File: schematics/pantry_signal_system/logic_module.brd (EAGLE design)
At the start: 45.7 x 53 mm, 24 parts, among them J5 JST-XH254-3P, J6 JST-XH254-2P, J7 JST-XH254-2P, Q4 STP14NM50N, Q5 2N3904, U10 FAN73611, U11 ATMEGA328P, U12 E220-900T22D, U13 BME280BME280-CONNECTOR-ONLY, U14 2004A I2C

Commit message: 1. Fixed issues in boards and firmwares
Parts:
- added J10: USBASP_PIN, my_devices:USBASP_PIN
- moved R24 13.0 mm to (63.5, 48.3), turned to 180 degrees
- moved FS1 8.03 mm to (67.3, 53.3), turned to 180 degrees
- moved FS2 4.02 mm to (58.4, 53.3)
- moved R23 2.54 mm to (45.7, 69.8)
- moved R26 1.27 mm to (63.5, 44.5)
- moved U13 1.27 mm to (68.6, 64.8)
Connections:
- removed net N$7: C9.P$1, R21.P$1, U11.PC6
- new net RESET: C9.P$1, J10.RST, R21.P$1, U11.PC6
- new net SERIAL_RX: J10.RXD, U11.PD1
- new net SERIAL_TX: J10.TXD, U11.PD0
- net +5V: now also J10.VCC
- net GND: now also J10.GND, J10.GND1
- net I2C2_SCL: now also J10.SCK
- net I2C2_SDA: now also J10.MISO
- net I2C_SCL: now also U11.PC5; no longer U11.PC4
- net I2C_SDA: now also U11.PC4; no longer U11.PC5
- net OPEN_DOOR_ALARM: now also J10.MOSI
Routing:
- net I2C2_SCL: track 9.20 -> 50.9 mm
- net RESET: track 0.00 -> 40.8 mm
- net I2C2_SDA: track 5.61 -> 43.9 mm
- net OPEN_DOOR_ALARM: track 22.5 -> 60.4 mm
- net SERIAL_TX: track 0.00 -> 34.2 mm, vias 0 -> 1
- net N$7: track 20.4 -> 0.00 mm
- net SERIAL_RX: track 0.00 -> 19.4 mm, vias 0 -> 1
- net GND: track 186.3 -> 175.3 mm
- net FLOODING_ALARM_OUTDOOR: track 12.5 -> 23.2 mm
- net I2C_SDA: track 15.5 -> 21.9 mm
- net +5V: track 135.9 -> 142.2 mm
- net LORA_RX: track 11.7 -> 16.5 mm
- net FLOODING_ALARM_INDOOR: track 14.1 -> 16.1 mm
- net I2C_SCL: track 19.6 -> 18.6 mm
- net ENABLE_DISPLAY: track 19.1 -> 19.9 mm
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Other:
- board text added: "REQ"
- board text added: "TX"

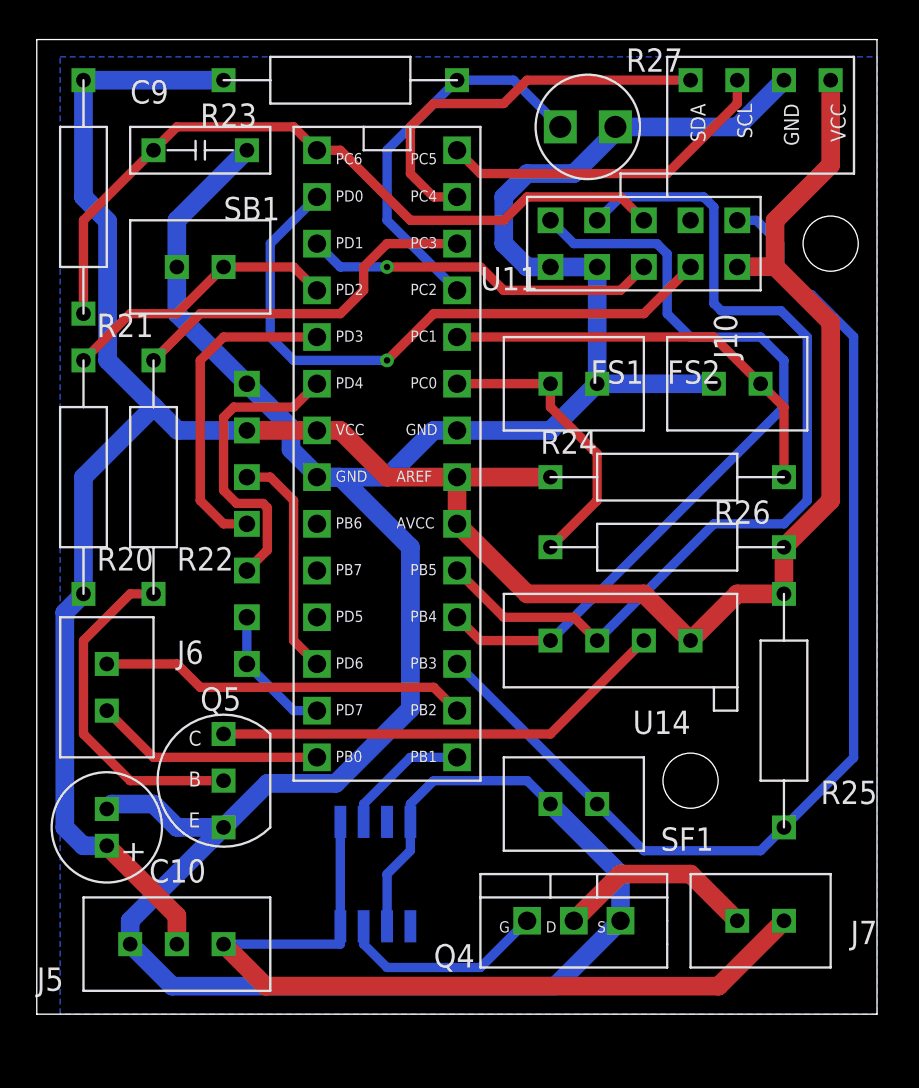
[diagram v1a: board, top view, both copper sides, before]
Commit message: Changes in schematics, changes in source code. Current version works too, but I changed boards to fix some possible errors
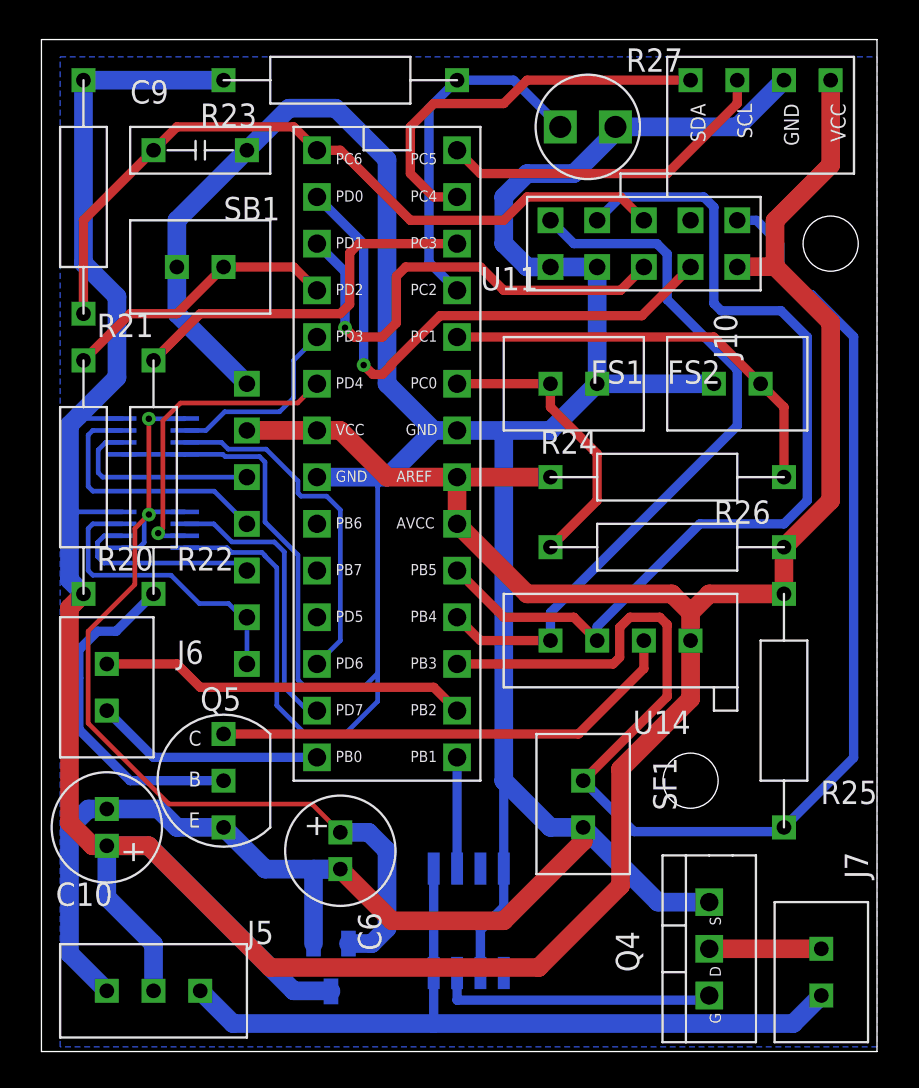
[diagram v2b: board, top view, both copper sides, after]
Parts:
- added C6: 10 uF, my_devices:C-MINI-5X7
- added U2, U3: SN74LVC2T45DCUR, my_devices:VSSOP-8
- added U7: MCP1703T-3302E/CB, my_devices:SOT-23A
- moved Q4 7.52 mm to (65.8, 22.6), turned to 90 degrees
- moved U10 5.68 mm to (52.1, 24.1)
- moved J7 4.33 mm to (71.9, 21.3), turned to 90 degrees
- moved J5 2.84 mm to (35.6, 20.3)
- moved SF1 0.51 mm to (58.9, 30.5), turned to 270 degrees
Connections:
- new net 3V3: C6.PLUS, U2.P1, U2.P5, U3.P1, U7.P2
- new net N$1: U12.TX, U3.P7
- new net N$2: U12.RX, U2.P6
- new net N$3: U12.AUX, U3.P6
- new net N$9: U12.M0, U12.M1, U2.P7
- net +5V: now also U2.P8, U3.P8, U7.P3
- net GND: now also C6.MINUS, U2.P4, U3.P4, U3.P5, U7.P1
- net LORA_AUX: now also U3.P3; no longer U12.AUX
- net LORA_M0M1: now also U2.P2; no longer U12.M0, U12.M1
- net LORA_RX: now also U2.P3; no longer U12.RX
- net LORA_TX: now also U3.P2; no longer U12.TX
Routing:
- net GND: track 175.3 -> 247.8 mm
- net +5V: track 142.2 -> 205.6 mm
- net 3V3: track 0.00 -> 50.6 mm, vias 0 -> 2
- net N$9: track 0.00 -> 16.6 mm
- net N$1: track 0.00 -> 14.2 mm
- net OPEN_DOOR_ALARM: track 60.4 -> 74.0 mm
- net N$3: track 0.00 -> 10.9 mm
- net N$2: track 0.00 -> 10.7 mm
- net LORA_M0M1: track 7.40 -> 15.7 mm
- net LORA_TX: track 17.6 -> 10.5 mm
- net LORA_AUX: track 12.5 -> 19.3 mm
- net SERIAL_RX: track 19.4 -> 25.8 mm
- net N$4: track 11.0 -> 6.10 mm
- net I2C2_SDA: track 43.9 -> 39.5 mm
- net N$6: track 11.4 -> 15.3 mm
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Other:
- board size 45.7 x 53 mm -> 45.4 x 55 mm

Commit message: Debugging logic module firmware, estabilishing LoRa connection....
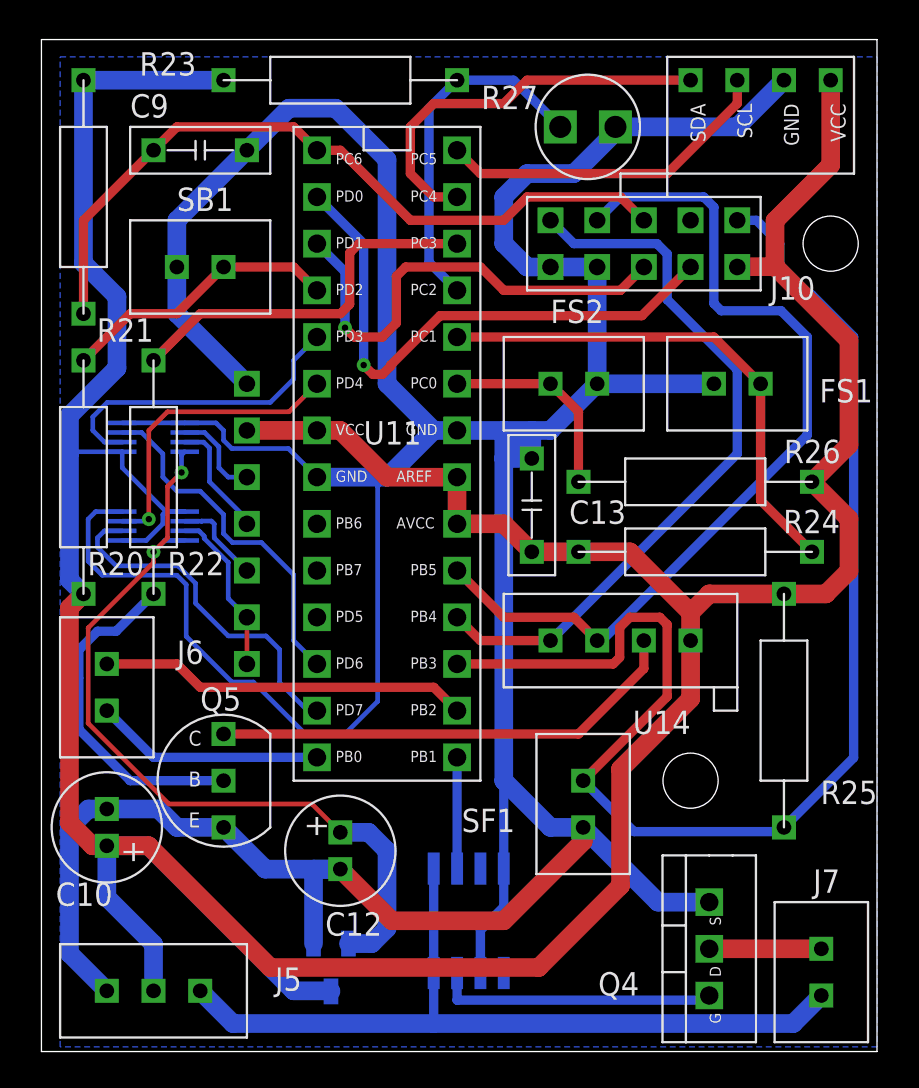
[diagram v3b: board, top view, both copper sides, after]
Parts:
- removed U2, U3: SN74LVC2T45DCUR, my_devices:VSSOP-8
- added C13: 100 nF, my_devices:C-1
- added U16, U17: SN74LVC2T45DCUR, my_devices:VSSOP-8
- moved R24 4.34 mm to (65.0, 44.2)
- moved R26 3.87 mm to (65.0, 48.0)
- renumbered C6 to C12, U7 to U15
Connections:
- net +5V: now also C13.P$2, U16.P1, U16.P5, U17.P1; no longer U2.P8, U3.P8
- net 3V3: now also U16.P8, U17.P8; no longer U2.P1, U2.P5, U3.P1
- net GND: now also C13.P$1, U16.P4, U17.P4, U17.P5; no longer U2.P4, U3.P4, U3.P5
- net LORA_AUX: now also U17.P3; no longer U3.P3
- net LORA_M0M1: now also U16.P2; no longer U2.P2
- net LORA_RX: now also U16.P3; no longer U2.P3
- net LORA_TX: now also U17.P2; no longer U3.P2
- net N$1: now also U17.P7; no longer U3.P7
- net N$2: now also U16.P6; no longer U2.P6
- net N$3: now also U17.P6; no longer U3.P6
- net N$9: now also U16.P7; no longer U2.P7
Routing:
- net N$1: track 14.2 -> 6.45 mm
- net N$9: track 16.6 -> 9.09 mm
- net LORA_TX: track 10.5 -> 17.2 mm
- net +5V: track 205.6 -> 211.5 mm
- net 3V3: track 50.6 -> 44.7 mm
- net N$3: track 10.9 -> 5.05 mm
- net N$2: track 10.7 -> 4.95 mm
- net FLOODING_ALARM_INDOOR: track 16.1 -> 11.0 mm
- net FLOODING_ALARM_OUTDOOR: track 23.2 -> 27.9 mm
- net LORA_M0M1: track 15.7 -> 19.3 mm
- net GND: track 247.8 -> 245.2 mm
- net I2C2_SCL: track 51.3 -> 48.8 mm
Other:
- board text added: "U16"

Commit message: Capacitor nominal changed in logic-module to fix problem with chip restart when LoRa sends data with high current consumption
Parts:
- C10: value 10 uF -> 22000 uF
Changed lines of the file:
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@@
 <drawing>
 <settings>
-<setting alwaysvectorfont="yes"/>
+<setting alwaysvectorfont="no"/>
 <setting verticaltext="up"/>
 </settings>
@@
 </autorouter>
 <elements>
-<element name="C10" library="my_devices" package="C-MINI-5X7" value="10 uF" x="33.02" y="29.21" smashed="yes" rot="R90">
+<element name="C10" library="my_devices" package="C-MINI-5X7" value="22000 uF" x="33.02" y="29.21" smashed="yes" rot="R90">
 <attribute name="NAME" x="33.33" y="26.21" size="1.27" layer="21" rot="R180"/>
 </element>
